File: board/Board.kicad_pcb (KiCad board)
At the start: 2 copper layers, 50 x 50 mm, 59 parts, among them J1 GS3, J10 CONN_01X03, J11 CONN_01X03, J12 GS3, J13 GS3, J14 CONN_01X02, J15 CONN_01X03, J16 GS2, J17 CONN_01X01, J2 CONN_02X04, J3 CONN_01X03, J4 CONN_01X03, J5 CONN_01X03, J6 CONN_01X03, J7 CONN_01X03, J8 CONN_01X03, J9 CONN_01X03, SW1 SW_Push, U1 STM32F410RBTx, U2 SN74LVC1G04, U3 LF33ABDT-TR, U4 ICM-20689, U5 MAG3110, U6 MS5637, Y1 25 MHz

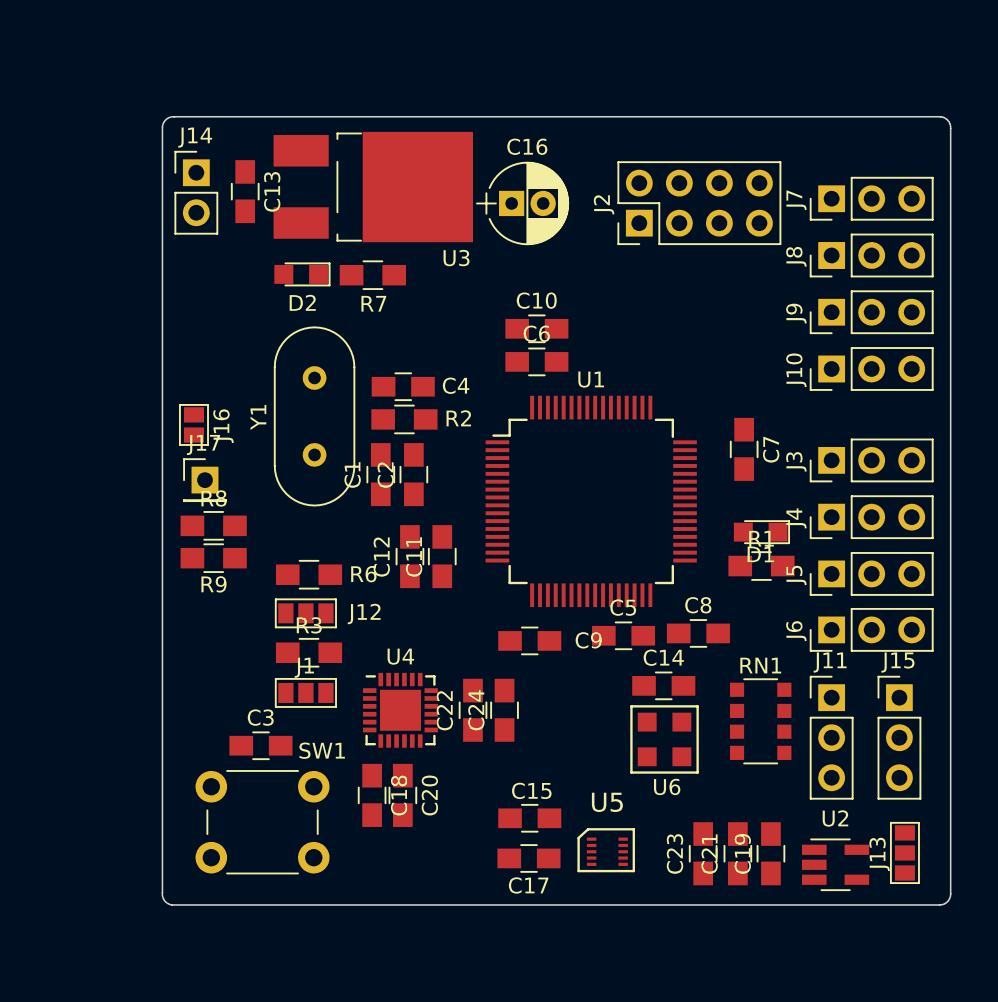
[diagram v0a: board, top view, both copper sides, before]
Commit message: mounting holes
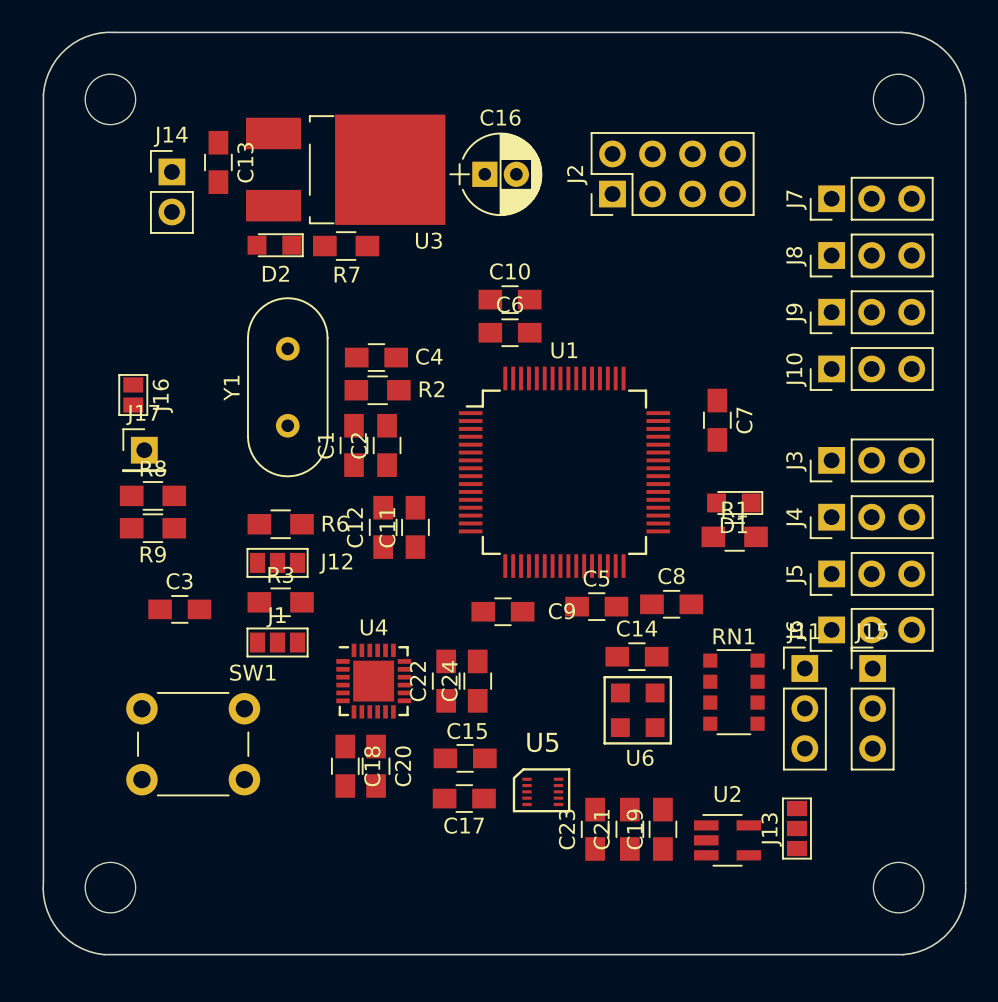
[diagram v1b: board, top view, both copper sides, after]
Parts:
- added ?: MountingHole_3.2mm_M3, Mounting_Holes:MountingHole_3.2mm_M3, F.Cu at (150.0, 70.0)
- added ?: MountingHole_3.2mm_M3, Mounting_Holes:MountingHole_3.2mm_M3, F.Cu at (100.0, 70.0)
- added ?: MountingHole_3.2mm_M3, Mounting_Holes:MountingHole_3.2mm_M3, F.Cu at (150.0, 120.0)
- added ?: MountingHole_3.2mm_M3, Mounting_Holes:MountingHole_3.2mm_M3, F.Cu at (100.0, 120.0)
- moved C3 10.1 mm to (104.4, 102.3)
- moved C21 7.02 mm to (132.9, 116.3)
- moved C19 7.02 mm to (135.1, 116.3)
- moved C23 7.02 mm to (130.8, 116.3)
- moved J13 7.02 mm to (143.6, 116.2)
- moved U2 7.02 mm to (139.2, 117.0)
- moved SW1 6.62 mm to (102.0, 108.7)
- moved C17 5.59 mm to (122.5, 114.3)
- moved C15 5.59 mm to (122.5, 111.8)
- moved U5 5.59 mm to (127.4, 114.0)
- moved J16 4.29 mm to (101.5, 88.8)
- moved J17 4.29 mm to (102.2, 92.2)
- moved R8 4.29 mm to (102.7, 95.2)
- moved R9 4.29 mm to (102.7, 97.2)
- moved J1 3.67 mm to (110.6, 104.5)
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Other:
- board size 50 x 50 mm -> 58.5 x 58.5 mm

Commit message: a bit of reorganization
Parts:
- moved R7 10.3 mm to (105.6, 83.7)
- moved C17 8.58 mm to (116.8, 120.8)
- moved U5 8.58 mm to (121.8, 120.5)
- moved C15 8.58 mm to (116.9, 118.3)
- moved D2 5.61 mm to (105.2, 81.3), turned to 0 degrees
- moved J17 5.59 mm to (99.7, 87.2)
- moved C14 5.55 mm to (129.6, 109.3)
- moved U6 5.55 mm to (129.6, 112.8)
- moved J16 5.35 mm to (99.3, 83.8), turned to 90 degrees
- moved R8 5.32 mm to (100.2, 90.5)
- moved J14 5.04 mm to (99.7, 77.3)
- moved R9 4.97 mm to (100.2, 92.9)
- moved RN1 4.44 mm to (136.9, 111.2)
- moved C3 4.37 mm to (100.6, 104.5)
- moved J12 4.06 mm to (106.8, 97.8)
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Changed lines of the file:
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@@
   )
   (module Capacitors_SMD:C_0805_HandSoldering (layer F.Cu)
-    (at 104.4 102.35)
+    (at 100.6 104.5)
     (descr "Capacitor SMD 0805, hand soldering")
     (tags "capacitor 0805")
@@
   )
   (module Capacitors_SMD:C_0805_HandSoldering (layer F.Cu)
-    (at 130.85 102.175)
+    (at 130.85 102.5)
     (descr "Capacitor SMD 0805, hand soldering")
     (tags "capacitor 0805")
@@
   )
   (module Capacitors_SMD:C_0805_HandSoldering (layer F.Cu)
-    (at 135.6 102.025)
+    (at 135.7 102.5)
     (descr "Capacitor SMD 0805, hand soldering")
     (tags "capacitor 0805")
@@
   )
   (module Capacitors_SMD:C_0805_HandSoldering (layer F.Cu)
-    (at 106.85 74 270)
+    (at 104.7 76.9 270)
     (descr "Capacitor SMD 0805, hand soldering")
     (tags "capacitor 0805")
@@
   )
   (module Capacitors_SMD:C_0805_HandSoldering (layer F.Cu)
-    (at 133.4 105.35)
+    (at 129.55 109.35)
     (descr "Capacitor SMD 0805, hand soldering")
     (tags "capacitor 0805")
@@
   )
   (module Capacitors_SMD:C_0805_HandSoldering (layer F.Cu)
-    (at 122.5 111.8 180)
+    (at 116.9 118.3 180)
     (descr "Capacitor SMD 0805, hand soldering")
     (tags "capacitor 0805")
@@
   )
   (module Capacitors_ThroughHole:CP_Radial_D5.0mm_P2.00mm (layer F.Cu)
-    (at 123.75 74.75)
+    (at 124.35 74.75)
     (descr "CP, Radial series, Radial, pin pitch=2.00mm, , diameter=5mm, Electrolytic Capacitor")
     (tags "CP Radial series Radial pin pitch 2.00mm  diameter 5mm Electrolytic Capacitor")
@@
   )
   (module Capacitors_SMD:C_0805_HandSoldering (layer F.Cu)
-    (at 122.45 114.35 180)
+    (at 116.85 120.85 180)
     (descr "Capacitor SMD 0805, hand soldering")
     (tags "capacitor 0805")
@@
   )
   (module Capacitors_SMD:C_0805_HandSoldering (layer F.Cu)
-    (at 114.9 112.3 270)
+    (at 112.8 112.75 270)
     (descr "Capacitor SMD 0805, hand soldering")
     (tags "capacitor 0805")
@@
   )
   (module Capacitors_SMD:C_0805_HandSoldering (layer F.Cu)
-    (at 135.05 116.3 90)
+    (at 134.25 119.6 90)
     (descr "Capacitor SMD 0805, hand soldering")
     (tags "capacitor 0805")
@@
   )
   (module Capacitors_SMD:C_0805_HandSoldering (layer F.Cu)
-    (at 116.85 112.3 270)
+    (at 114.75 112.75 270)
     (descr "Capacitor SMD 0805, hand soldering")
     (tags "capacitor 0805")
@@
   )
   (module Capacitors_SMD:C_0805_HandSoldering (layer F.Cu)
-    (at 132.95 116.3 90)
+    (at 132.15 119.6 90)
     (descr "Capacitor SMD 0805, hand soldering")
     (tags "capacitor 0805")
@@
   )
   (module Capacitors_SMD:C_0805_HandSoldering (layer F.Cu)
-    (at 121.3 106.9 90)
+    (at 118.95 106.5 90)
     (descr "Capacitor SMD 0805, hand soldering")
     (tags "capacitor 0805")
@@
   )
   (module Capacitors_SMD:C_0805_HandSoldering (layer F.Cu)
-    (at 130.75 116.3 90)
+    (at 129.95 119.6 90)
     (descr "Capacitor SMD 0805, hand soldering")
     (tags "capacitor 0805")
@@
   )
   (module LEDs:LED_0805 (layer F.Cu)
-    (at 110.4 79.25 180)
+    (at 105.2 81.35)
     (descr "LED 0805 smd package")
     (tags "LED led 0805 SMD smd SMT smt smdled SMDLED smtled SMTLED")
     (attr smd)
-    (fp_text reference D2 (at -0.1 -1.85 180) (layer F.SilkS)
-      (effects (font (size 1 1) (thickness 0.15)))
-    )
-    (fp_text value LED (at 0 1.55 180) (layer F.Fab)
+    (fp_text reference D2 (at -0.1 -1.85) (layer F.SilkS)
+      (effects (font (size 1 1) (thickness 0.15)))
+    )
+    (fp_text value LED (at 0 1.55) (layer F.Fab)
       (effects (font (size 1 1) (thickness 0.15)))
     )
@@
     (fp_line (start -1.95 0.85) (end -1.95 -0.85) (layer F.CrtYd) (width 0.05))
     (fp_line (start -1.95 -0.85) (end 1.95 -0.85) (layer F.CrtYd) (width 0.05))
-    (pad 2 smd rect (at 1.1 0) (size 1.2 1.2) (layers F.Cu F.Paste F.Mask)
-      (net 5 VCC))
-    (pad 1 smd rect (at -1.1 0) (size 1.2 1.2) (layers F.Cu F.Paste F.Mask)
+    (pad 2 smd rect (at 1.1 0 180) (size 1.2 1.2) (layers F.Cu F.Paste F.Mask)
+      (net 5 VCC))
+    (pad 1 smd rect (at -1.1 0 180) (size 1.2 1.2) (layers F.Cu F.Paste F.Mask)
       (net 13 "Net-(D2-Pad1)"))
     (model LEDs.3dshapes/LED_0805.wrl
@@
   )
   (module Connect:GS3 (layer F.Cu)
-    (at 110.6 104.45 270)
+    (at 106.85 102.9 270)
     (descr "3-pin solder bridge")
     (tags "solder bridge")
@@
   )
   (module Pin_Headers:Pin_Header_Straight_2x04_Pitch2.54mm (layer F.Cu)
-    (at 131.85 76 90)
+    (at 132.1 76 90)
     (descr "Through hole straight pin header, 2x04, 2.54mm pitch, double rows")
     (tags "Through hole pin header THT 2x04 2.54mm double row")
@@
   )
   (module Connect:GS3 (layer F.Cu)
-    (at 110.6 99.4 270)
+    (at 106.85 97.85 270)
     (descr "3-pin solder bridge")
     (tags "solder bridge")
@@
   )
   (module Connect:GS3 (layer F.Cu)
-    (at 143.55 116.25)
+    (at 142.75 119.55)
     (descr "3-pin solder bridge")
     (tags "solder bridge")
@@
   )
   (module Pin_Headers:Pin_Header_Straight_1x02_Pitch2.54mm (layer F.Cu)
-    (at 103.9 74.6)
+    (at 99.65 77.3)
     (descr "Through hole straight pin header, 1x02, 2.54mm pitch, single row")
     (tags "Through hole pin header THT 1x02 2.54mm single row")
@@
   )
   (module Connect:GS2 (layer F.Cu)
-    (at 101.45 88.75)
+    (at 99.3 83.85 90)
     (descr "2-pin solder bridge")
     (tags "solder bridge")
     (attr smd)
-    (fp_text reference J16 (at 1.78 0 90) (layer F.SilkS)
-      (effects (font (size 1 1) (thickness 0.15)))
-    )
-    (fp_text value GS2 (at -1.8 0 90) (layer F.Fab)
+    (fp_text reference J16 (at 1.78 0 180) (layer F.SilkS)
+      (effects (font (size 1 1) (thickness 0.15)))
+    )
+    (fp_text value GS2 (at -1.8 0 180) (layer F.Fab)
       (effects (font (size 1 1) (thickness 0.15)))
     )
@@
     (fp_line (start 0.89 1.27) (end -0.89 1.27) (layer F.SilkS) (width 0.12))
     (fp_line (start -0.89 -1.27) (end 0.89 -1.27) (layer F.SilkS) (width 0.12))
-    (pad 1 smd rect (at 0 -0.64) (size 1.27 0.97) (layers F.Cu F.Paste F.Mask)
+    (pad 1 smd rect (at 0 -0.64 90) (size 1.27 0.97) (layers F.Cu F.Paste F.Mask)
       (net 7 +BATT))
-    (pad 2 smd rect (at 0 0.64) (size 1.27 0.97) (layers F.Cu F.Paste F.Mask)
+    (pad 2 smd rect (at 0 0.64 90) (size 1.27 0.97) (layers F.Cu F.Paste F.Mask)
       (net 41 "Net-(J16-Pad2)"))
   )
   (module Pin_Headers:Pin_Header_Straight_1x01_Pitch2.54mm (layer F.Cu)
-    (at 102.15 92.25)
+    (at 99.65 87.25)
     (descr "Through hole straight pin header, 1x01, 2.54mm pitch, single row")
     (tags "Through hole pin header THT 1x01 2.54mm single row")
@@
   )
   (module Resistors_SMD:R_0805_HandSoldering (layer F.Cu)
-    (at 110.8 101.9)
+    (at 107.05 100.35)
     (descr "Resistor SMD 0805, hand soldering")
     (tags "resistor 0805")
@@
   )
   (module Resistors_SMD:R_0805_HandSoldering (layer F.Cu)
-    (at 110.8 96.95 180)
+    (at 107.05 95.4 180)
     (descr "Resistor SMD 0805, hand soldering")
     (tags "resistor 0805")
@@
   )
   (module Resistors_SMD:R_0805_HandSoldering (layer F.Cu)
-    (at 114.95 79.3)
+    (at 105.6 83.65)
     (descr "Resistor SMD 0805, hand soldering")
     (tags "resistor 0805")
@@
   )
   (module Resistors_SMD:R_0805_HandSoldering (layer F.Cu)
-    (at 102.7 95.15)
+    (at 100.2 90.45)
     (descr "Resistor SMD 0805, hand soldering")
     (tags "resistor 0805")
@@
   )
   (module Resistors_SMD:R_0805_HandSoldering (layer F.Cu)
-    (at 102.7 97.2 180)
+    (at 100.2 92.9 180)
     (descr "Resistor SMD 0805, hand soldering")
     (tags "resistor 0805")
@@
   )
   (module Buttons_Switches_ThroughHole:SW_PUSH_6mm (layer F.Cu)
-    (at 102 108.65)
+    (at 99.85 107.75)
     (descr https://www.omron.com/ecb/products/pdf/en-b3f.pdf)
     (tags "tact sw push 6mm")
@@
   )
   (module TO_SOT_Packages_SMD:SOT-23-5_HandSoldering (layer F.Cu)
-    (at 139.15 117)
+    (at 138.35 120.3)
     (descr "5-pin SOT23 package")
     (tags "SOT-23-5 hand-soldering")
@@
   )
   (module Housings_DFN_QFN:QFN-24-1EP_4x4mm_Pitch0.5mm (layer F.Cu)
-    (at 116.7 106.9)
+    (at 114.35 106.5)
     (descr "24-Lead Plastic Quad Flat, No Lead Package (MJ) - 4x4x0.9 mm Body [QFN]; (see Microchip Packaging Specification 00000049BS.pdf)")
     (tags "QFN 0.5")
@@
   )
   (module Local_prints:DFN_2x2mm_10pin_0.4pitch (layer F.Cu)
-    (at 127.4 113.95)
+    (at 121.8 120.45)
     (fp_text reference U5 (at 0.025 -3.125) (layer F.SilkS)
       (effects (font (size 1.2 1.2) (thickness 0.15)))
@@
   )
   (module Local_prints:MS5637 (layer F.Cu)
-    (at 133.45 108.75)
+    (at 129.6 112.75)
     (fp_text reference U6 (at 0.15 3.05) (layer F.SilkS)
       (effects (font (size 1 1) (thickness 0.15)))
@@
   )
   (module Resistors_SMD:R_Array_Convex_4x1206 (layer F.Cu)
-    (at 139.55 107.6)
+    (at 136.95 111.2)
     (descr "Chip Resistor Network, ROHM MNR34 (see mnr_g.pdf)")
     (tags "resistor array")

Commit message: started routing
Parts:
- moved C4 4.97 mm to (121.0, 83.6), turned to 90 degrees
- moved C2 2.80 mm to (116.8, 94.7)
- moved Y1 2.80 mm to (112.0, 93.4)
- moved C1 2.78 mm to (116.8, 89.5)
- moved C12 2.65 mm to (116.8, 99.8)
- moved C11 2.63 mm to (119.0, 99.8)
- moved R2 2.31 mm to (119.0, 89.6), turned to 270 degrees
- moved C5 2.18 mm to (131.6, 104.5), turned to 270 degrees
- moved R6 1.69 mm to (105.7, 94.5)
- moved J1 1.48 mm to (105.5, 102.2)
- moved J12 1.48 mm to (105.5, 97.2)
- moved R3 1.48 mm to (105.8, 99.7)
- moved J14 1.32 mm to (100.2, 76.1)
- moved J16 1.32 mm to (99.8, 82.7)
- moved J17 1.10 mm to (100.2, 86.3)
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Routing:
- net VCC: track 0.00 -> 104.2 mm
- net GND: track 0.00 -> 45.5 mm, vias 0 -> 9
- net BATT_ADC: track 0.00 -> 27.0 mm, vias 0 -> 2
- net +BATT: track 0.00 -> 20.3 mm
- net Net-(C2-Pad2): track 0.00 -> 11.3 mm
- net Net-(J16-Pad2): track 0.00 -> 7.85 mm
- net Net-(C1-Pad2): track 0.00 -> 7.06 mm
- net Net-(R2-Pad2): track 0.00 -> 4.29 mm
- net Net-(C5-Pad1): track 0.00 -> 3.72 mm
- net Net-(D2-Pad1): track 0.00 -> 2.36 mm
- added copper zone on B.Cu, net GND
